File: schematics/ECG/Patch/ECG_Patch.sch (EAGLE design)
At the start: 7 parts

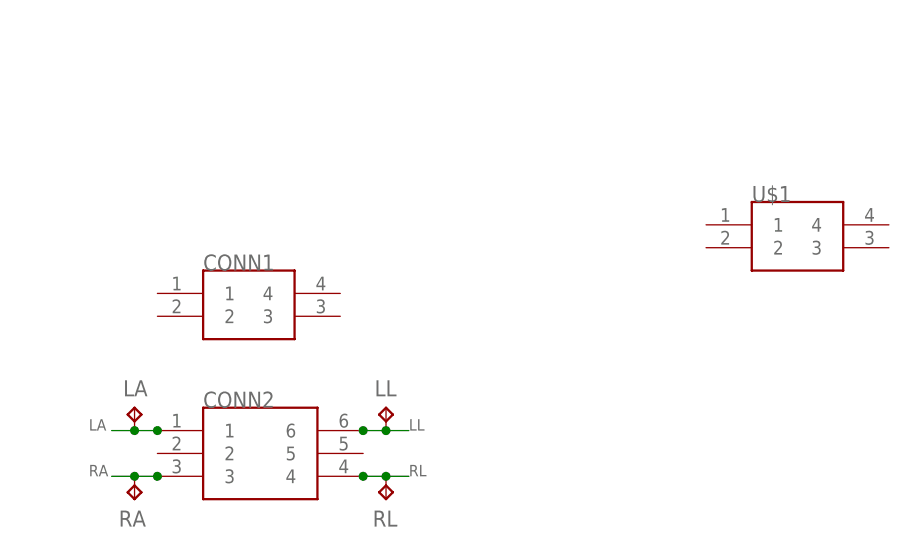
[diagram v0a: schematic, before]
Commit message: changed 4 pin to through hole and added v1.0 marking
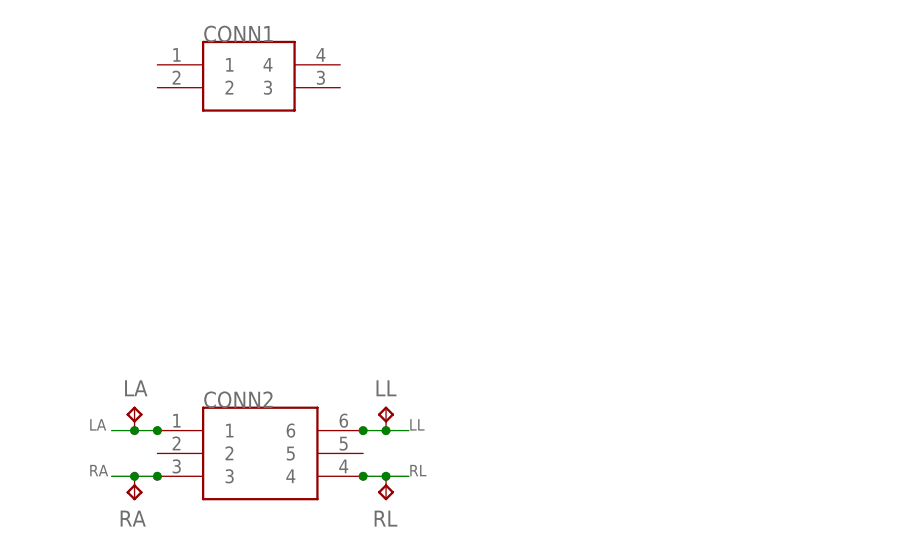
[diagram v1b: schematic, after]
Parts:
- removed U$1: M80-4SMT, harwin:M80-4SMT
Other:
- moved on the sheet: CONN1
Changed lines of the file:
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@@
 </classes>
 <parts>
-<part name="CONN1" library="harwin" deviceset="M80-4" device="V"/>
 <part name="CONN2" library="harwin" deviceset="M80-6" device="V"/>
 <part name="LL" library="testpad" deviceset="TP" device="TP20R"/>
@@
 <part name="RA" library="testpad" deviceset="TP" device="TP20R"/>
 <part name="RL" library="testpad" deviceset="TP" device="TP20R"/>
-<part name="U$1" library="harwin" deviceset="M80-4" device="SMT"/>
+<part name="CONN1" library="harwin" deviceset="M80-4" device="V"/>
 </parts>
 <sheets>
@@
 </plain>
 <instances>
-<instance part="CONN1" gate="CONN" x="22.86" y="55.88"/>
 <instance part="CONN2" gate="CONN" x="22.86" y="40.64"/>
 <instance part="LL" gate="G$1" x="38.1" y="45.72"/>
@@
 <instance part="RA" gate="G$1" x="10.16" y="35.56" rot="R180"/>
 <instance part="RL" gate="G$1" x="38.1" y="35.56" rot="R180"/>
-<instance part="U$1" gate="CONN" x="83.82" y="63.5"/>
+<instance part="CONN1" gate="CONN" x="22.86" y="81.28"/>
 </instances>
 <busses>

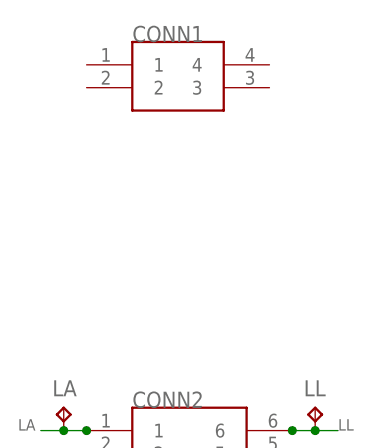
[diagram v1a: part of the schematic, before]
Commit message: switched ECG boards to spring loaded pin headers
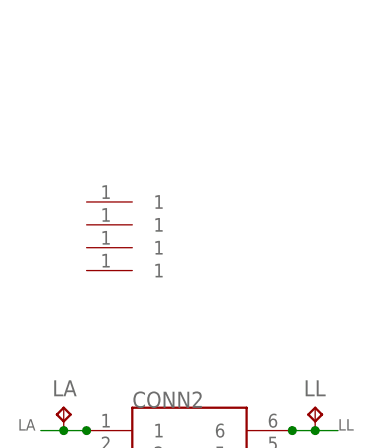
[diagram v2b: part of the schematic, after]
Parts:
- removed CONN1: M80-4V, harwin:M80-4V
- added U$1, U$2, U$3, U$4: PISTON_RA_TH, pins:PISTON_RA_TH
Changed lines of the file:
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@@
 <?xml version="1.0" encoding="utf-8"?>
 <!DOCTYPE eagle SYSTEM "eagle.dtd">
-<eagle version="6.4">
+<eagle version="6.5.0">
 <drawing>
 <settings>
@@
 <part name="RA" library="testpad" deviceset="TP" device="TP20R"/>
 <part name="RL" library="testpad" deviceset="TP" device="TP20R"/>
-<part name="CONN1" library="harwin" deviceset="M80-4" device="V"/>
+<part name="U$1" library="pins" deviceset="PISTON_RA_TH" device=""/>
+<part name="U$2" library="pins" deviceset="PISTON_RA_TH" device=""/>
+<part name="U$3" library="pins" deviceset="PISTON_RA_TH" device=""/>
+<part name="U$4" library="pins" deviceset="PISTON_RA_TH" device=""/>
 </parts>
 <sheets>
@@
 <instance part="RA" gate="G$1" x="10.16" y="35.56" rot="R180"/>
 <instance part="RL" gate="G$1" x="38.1" y="35.56" rot="R180"/>
-<instance part="CONN1" gate="CONN" x="22.86" y="81.28"/>
+<instance part="U$1" gate="PIN" x="17.78" y="66.04"/>
+<instance part="U$2" gate="PIN" x="17.78" y="68.58"/>
+<instance part="U$3" gate="PIN" x="17.78" y="63.5"/>
+<instance part="U$4" gate="PIN" x="17.78" y="60.96"/>
 </instances>
 <busses>

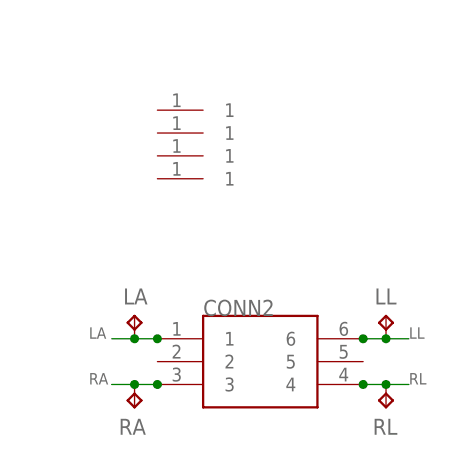
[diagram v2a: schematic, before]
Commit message: redesigned patch board and charging board
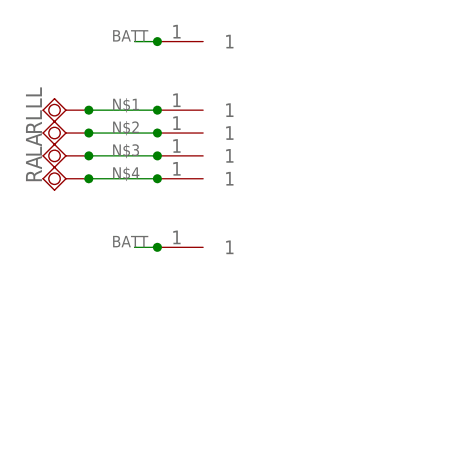
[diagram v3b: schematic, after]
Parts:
- removed CONN2: M80-6V, harwin:M80-6V
- added U$5, U$6: PISTON_RA_TH, pins:PISTON_RA_TH
- LA, LL, RA, RL: value TPTP20R -> TPSQPAD1-20; device testpad:TPTP20R -> testpad:TPSQPAD1-20
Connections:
- removed net LA: CONN2.1, LA.TP
- removed net LL: CONN2.6, LL.TP
- removed net RA: CONN2.3, RA.TP
- removed net RL: CONN2.4, RL.TP
- new net BATT: U$5.1, U$6.1
- new net N$1: LL.TP, U$2.1
- new net N$2: RL.TP, U$1.1
- new net N$3: LA.TP, U$3.1
- new net N$4: RA.TP, U$4.1
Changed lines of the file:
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@@
 </classes>
 <parts>
-<part name="CONN2" library="harwin" deviceset="M80-6" device="V"/>
-<part name="LL" library="testpad" deviceset="TP" device="TP20R"/>
-<part name="LA" library="testpad" deviceset="TP" device="TP20R"/>
-<part name="RA" library="testpad" deviceset="TP" device="TP20R"/>
-<part name="RL" library="testpad" deviceset="TP" device="TP20R"/>
 <part name="U$1" library="pins" deviceset="PISTON_RA_TH" device=""/>
 <part name="U$2" library="pins" deviceset="PISTON_RA_TH" device=""/>
 <part name="U$3" library="pins" deviceset="PISTON_RA_TH" device=""/>
 <part name="U$4" library="pins" deviceset="PISTON_RA_TH" device=""/>
+<part name="LL" library="testpad" deviceset="TPSQ" device="PAD1-20"/>
+<part name="RL" library="testpad" deviceset="TPSQ" device="PAD1-20"/>
+<part name="LA" library="testpad" deviceset="TPSQ" device="PAD1-20"/>
+<part name="RA" library="testpad" deviceset="TPSQ" device="PAD1-20"/>
+<part name="U$5" library="pins" deviceset="PISTON_RA_TH" device=""/>
+<part name="U$6" library="pins" deviceset="PISTON_RA_TH" device=""/>
 </parts>
 <sheets>
@@
 </plain>
 <instances>
-<instance part="CONN2" gate="CONN" x="22.86" y="40.64"/>
-<instance part="LL" gate="G$1" x="38.1" y="45.72"/>
-<instance part="LA" gate="G$1" x="10.16" y="45.72"/>
-<instance part="RA" gate="G$1" x="10.16" y="35.56" rot="R180"/>
-<instance part="RL" gate="G$1" x="38.1" y="35.56" rot="R180"/>
 <instance part="U$1" gate="PIN" x="17.78" y="66.04"/>
 <instance part="U$2" gate="PIN" x="17.78" y="68.58"/>
 <instance part="U$3" gate="PIN" x="17.78" y="63.5"/>
 <instance part="U$4" gate="PIN" x="17.78" y="60.96"/>
+<instance part="LL" gate="G$1" x="2.54" y="68.58" rot="R270"/>
+<instance part="RL" gate="G$1" x="2.54" y="66.04" rot="R270"/>
+<instance part="LA" gate="G$1" x="2.54" y="63.5" rot="R270"/>
+<instance part="RA" gate="G$1" x="2.54" y="60.96" rot="R270"/>
+<instance part="U$5" gate="PIN" x="17.78" y="76.2"/>
+<instance part="U$6" gate="PIN" x="17.78" y="53.34"/>
 </instances>
 <busses>
 </busses>
 <nets>
-<net name="LA" class="0">
+<net name="N$1" class="0">
 <segment>
-<pinref part="CONN2" gate="CONN" pin="1"/>
-<junction x="12.7" y="43.18"/>
-<label x="5.08" y="43.18" size="1.27" layer="95"/>
-<pinref part="LA" gate="G$1" pin="TP"/>
-<wire x1="12.7" y1="43.18" x2="10.16" y2="43.18" width="0.1524" layer="91"/>
-<wire x1="10.16" y1="43.18" x2="7.62" y2="43.18" width="0.1524" layer="91"/>
-<junction x="10.16" y="43.18"/>
+<pinref part="U$2" gate="PIN" pin="1"/>
+<pinref part="LL" gate="G$1" pin="TP"/>
+<wire x1="12.7" y1="68.58" x2="5.08" y2="68.58" width="0.1524" layer="91"/>
+<junction x="5.08" y="68.58"/>
+<junction x="12.7" y="68.58"/>
+<label x="7.62" y="68.58" size="1.27" layer="95"/>
 </segment>
 </net>
-<net name="RL" class="0">
+<net name="N$2" class="0">
 <segment>
-<label x="40.64" y="38.1" size="1.27" layer="95"/>
+<pinref part="U$1" gate="PIN" pin="1"/>
 <pinref part="RL" gate="G$1" pin="TP"/>
-<wire x1="38.1" y1="38.1" x2="40.64" y2="38.1" width="0.1524" layer="91"/>
-<pinref part="CONN2" gate="CONN" pin="4"/>
-<wire x1="38.1" y1="38.1" x2="35.56" y2="38.1" width="0.1524" layer="91"/>
-<junction x="38.1" y="38.1"/>
-<junction x="35.56" y="38.1"/>
+<wire x1="12.7" y1="66.04" x2="5.08" y2="66.04" width="0.1524" layer="91"/>
+<junction x="5.08" y="66.04"/>
+<junction x="12.7" y="66.04"/>
+<label x="7.62" y="66.04" size="1.27" layer="95"/>
 </segment>
 </net>
-<net name="LL" class="0">
+<net name="N$3" class="0">
 <segment>
-<pinref part="CONN2" gate="CONN" pin="6"/>
-<wire x1="35.56" y1="43.18" x2="38.1" y2="43.18" width="0.1524" layer="91"/>
-<junction x="35.56" y="43.18"/>
-<label x="40.64" y="43.18" size="1.27" layer="95"/>
-<pinref part="LL" gate="G$1" pin="TP"/>
-<wire x1="38.1" y1="43.18" x2="40.64" y2="43.18" width="0.1524" layer="91"/>
-<junction x="38.1" y="43.18"/>
+<pinref part="U$3" gate="PIN" pin="1"/>
+<pinref part="LA" gate="G$1" pin="TP"/>
+<wire x1="12.7" y1="63.5" x2="5.08" y2="63.5" width="0.1524" layer="91"/>
+<junction x="5.08" y="63.5"/>
+<junction x="12.7" y="63.5"/>
+<label x="7.62" y="63.5" size="1.27" layer="95"/>
 </segment>
 </net>
-<net name="RA" class="0">
+<net name="N$4" class="0">
 <segment>
-<wire x1="10.16" y1="38.1" x2="7.62" y2="38.1" width="0.1524" layer="91"/>
+<pinref part="U$4" gate="PIN" pin="1"/>
 <pinref part="RA" gate="G$1" pin="TP"/>
-<label x="5.08" y="38.1" size="1.27" layer="95"/>
-<pinref part="CONN2" gate="CONN" pin="3"/>
-<wire x1="10.16" y1="38.1" x2="12.7" y2="38.1" width="0.1524" layer="91"/>
-<junction x="10.16" y="38.1"/>
-<junction x="12.7" y="38.1"/>
+<wire x1="12.7" y1="60.96" x2="5.08" y2="60.96" width="0.1524" layer="91"/>
+<junction x="5.08" y="60.96"/>
+<junction x="12.7" y="60.96"/>
+<label x="7.62" y="60.96" size="1.27" layer="95"/>
 </segment>
 </net>
+<net name="BATT" class="0">
+<segment>
+<pinref part="U$5" gate="PIN" pin="1"/>
+<wire x1="12.7" y1="76.2" x2="10.16" y2="76.2" width="0.1524" layer="91"/>
+<junction x="12.7" y="76.2"/>
+<label x="7.62" y="76.2" size="1.27" layer="95"/>
+</segment>
+<segment>
+<pinref part="U$6" gate="PIN" pin="1"/>
+<wire x1="12.7" y1="53.34" x2="10.16" y2="53.34" width="0.1524" layer="91"/>
+<junction x="12.7" y="53.34"/>
+<label x="7.62" y="53.34" size="1.27" layer="95"/>
+</segment>
+</net>

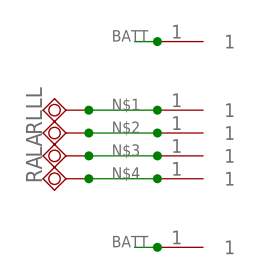
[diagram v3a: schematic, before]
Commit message: scaled down patch pcb. Same dimensions as charger board
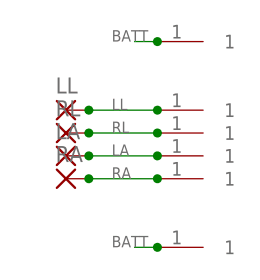
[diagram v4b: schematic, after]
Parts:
- LA, LL, RA, RL: value TPSQPAD1-20 -> (none); device testpad:TPSQPAD1-20 -> wirepad:1,6/0,8
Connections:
- removed net N$1: LL.TP, U$2.1
- removed net N$2: RL.TP, U$1.1
- removed net N$3: LA.TP, U$3.1
- removed net N$4: RA.TP, U$4.1
- new net LA: LA.P, U$3.1
- new net LL: LL.P, U$2.1
- new net RA: RA.P, U$4.1
- new net RL: RL.P, U$1.1
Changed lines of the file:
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@@
 <?xml version="1.0" encoding="utf-8"?>
 <!DOCTYPE eagle SYSTEM "eagle.dtd">
-<eagle version="6.5.0">
+<eagle version="6.4">
 <drawing>
 <settings>
@@
 <grid distance="0.1" unitdist="inch" unit="inch" style="lines" multiple="1" display="no" altdistance="0.01" altunitdist="inch" altunit="inch"/>
 <layers>
-<layer number="1" name="Top" color="4" fill="1" visible="no" active="no"/>
-<layer number="2" name="Route2" color="1" fill="3" visible="no" active="no"/>
-<layer number="3" name="Route3" color="4" fill="3" visible="no" active="no"/>
-<layer number="14" name="Route14" color="1" fill="6" visible="no" active="no"/>
-<layer number="15" name="Route15" color="4" fill="6" visible="no" active="no"/>
-<layer number="16" name="Bottom" color="1" fill="1" visible="no" active="no"/>
-<layer number="17" name="Pads" color="2" fill="1" visible="no" active="no"/>
-<layer number="18" name="Vias" color="2" fill="1" visible="no" active="no"/>
-<layer number="19" name="Unrouted" color="6" fill="1" visible="no" active="no"/>
-<layer number="20" name="Dimension" color="15" fill="1" visible="no" active="no"/>
-<layer number="21" name="tPlace" color="7" fill="1" visible="no" active="no"/>
-<layer number="22" name="bPlace" color="7" fill="1" visible="no" active="no"/>
-<layer number="23" name="tOrigins" color="15" fill="1" visible="no" active="no"/>
-<layer number="24" name="bOrigins" color="15" fill="1" visible="no" active="no"/>
-<layer number="25" name="tNames" color="7" fill="1" visible="no" active="no"/>
-<layer number="26" name="bNames" color="7" fill="1" visible="no" active="no"/>
-<layer number="27" name="tValues" color="7" fill="1" visible="no" active="no"/>
-<layer number="28" name="bValues" color="7" fill="1" visible="no" active="no"/>
+<layer number="1" name="Top" color="4" fill="1" visible="yes" active="no"/>
+<layer number="2" name="Route2" color="1" fill="3" visible="yes" active="no"/>
+<layer number="3" name="Route3" color="4" fill="3" visible="yes" active="no"/>
+<layer number="14" name="Route14" color="1" fill="6" visible="yes" active="no"/>
+<layer number="15" name="Route15" color="4" fill="6" visible="yes" active="no"/>
+<layer number="16" name="Bottom" color="1" fill="1" visible="yes" active="no"/>
+<layer number="17" name="Pads" color="2" fill="1" visible="yes" active="no"/>
+<layer number="18" name="Vias" color="2" fill="1" visible="yes" active="no"/>
+<layer number="19" name="Unrouted" color="6" fill="1" visible="yes" active="no"/>
+<layer number="20" name="Dimension" color="15" fill="1" visible="yes" active="no"/>
+<layer number="21" name="tPlace" color="7" fill="1" visible="yes" active="no"/>
+<layer number="22" name="bPlace" color="7" fill="1" visible="yes" active="no"/>
+<layer number="23" name="tOrigins" color="15" fill="1" visible="yes" active="no"/>
+<layer number="24" name="bOrigins" color="15" fill="1" visible="yes" active="no"/>
+<layer number="25" name="tNames" color="7" fill="1" visible="yes" active="no"/>
+<layer number="26" name="bNames" color="7" fill="1" visible="yes" active="no"/>
+<layer number="27" name="tValues" color="7" fill="1" visible="yes" active="no"/>
+<layer number="28" name="bValues" color="7" fill="1" visible="yes" active="no"/>
 <layer number="29" name="tStop" color="7" fill="3" visible="no" active="no"/>
 <layer number="30" name="bStop" color="7" fill="6" visible="no" active="no"/>
@@
 <layer number="35" name="tGlue" color="7" fill="4" visible="no" active="no"/>
 <layer number="36" name="bGlue" color="7" fill="5" visible="no" active="no"/>
-<layer number="37" name="tTest" color="7" fill="1" visible="no" active="no"/>
-<layer number="38" name="bTest" color="7" fill="1" visible="no" active="no"/>
+<layer number="37" name="tTest" color="7" fill="1" visible="yes" active="no"/>
+<layer number="38" name="bTest" color="7" fill="1" visible="yes" active="no"/>
 <layer number="39" name="tKeepout" color="4" fill="11" visible="no" active="no"/>
 <layer number="40" name="bKeepout" color="1" fill="11" visible="no" active="no"/>
@@
 <layer number="44" name="Drills" color="7" fill="1" visible="no" active="no"/>
 <layer number="45" name="Holes" color="7" fill="1" visible="no" active="no"/>
-<layer number="46" name="Milling" color="3" fill="1" visible="no" active="no"/>
-<layer number="47" name="Measures" color="7" fill="1" visible="no" active="no"/>
-<layer number="48" name="Document" color="7" fill="1" visible="no" active="no"/>
-<layer number="49" name="Reference" color="7" fill="1" visible="no" active="no"/>
-<layer number="50" name="dxf" color="7" fill="1" visible="no" active="no"/>
-<layer number="51" name="tDocu" color="7" fill="1" visible="no" active="no"/>
-<layer number="52" name="bDocu" color="7" fill="1" visible="no" active="no"/>
-<layer number="53" name="tGND_GNDA" color="7" fill="1" visible="no" active="no"/>
-<layer number="54" name="bGND_GNDA" color="7" fill="1" visible="no" active="no"/>
-<layer number="56" name="wert" color="7" fill="1" visible="no" active="no"/>
+<layer number="46" name="Milling" color="3" fill="1" visible="yes" active="no"/>
+<layer number="47" name="Measures" color="7" fill="1" visible="yes" active="no"/>
+<layer number="48" name="Document" color="7" fill="1" visible="yes" active="no"/>
+<layer number="49" name="Reference" color="7" fill="1" visible="yes" active="no"/>
+<layer number="50" name="dxf" color="7" fill="1" visible="yes" active="no"/>
+<layer number="51" name="tDocu" color="7" fill="1" visible="yes" active="no"/>
+<layer number="52" name="bDocu" color="7" fill="1" visible="yes" active="no"/>
+<layer number="53" name="tGND_GNDA" color="7" fill="1" visible="yes" active="no"/>
+<layer number="54" name="bGND_GNDA" color="7" fill="1" visible="yes" active="no"/>
+<layer number="56" name="wert" color="7" fill="1" visible="yes" active="no"/>
 <layer number="91" name="Nets" color="2" fill="1" visible="yes" active="yes"/>
 <layer number="92" name="Busses" color="1" fill="1" visible="yes" active="yes"/>
@@
 <part name="U$3" library="pins" deviceset="PISTON_RA_TH" device=""/>
 <part name="U$4" library="pins" deviceset="PISTON_RA_TH" device=""/>
-<part name="LL" library="testpad" deviceset="TPSQ" device="PAD1-20"/>
-<part name="RL" library="testpad" deviceset="TPSQ" device="PAD1-20"/>
-<part name="LA" library="testpad" deviceset="TPSQ" device="PAD1-20"/>
-<part name="RA" library="testpad" deviceset="TPSQ" device="PAD1-20"/>
 <part name="U$5" library="pins" deviceset="PISTON_RA_TH" device=""/>
 <part name="U$6" library="pins" deviceset="PISTON_RA_TH" device=""/>
+<part name="LL" library="wirepad" deviceset="1,6/0,8" device=""/>
+<part name="RL" library="wirepad" deviceset="1,6/0,8" device=""/>
+<part name="LA" library="wirepad" deviceset="1,6/0,8" device=""/>
+<part name="RA" library="wirepad" deviceset="1,6/0,8" device=""/>
 </parts>
 <sheets>
@@
 <instance part="U$3" gate="PIN" x="17.78" y="63.5"/>
 <instance part="U$4" gate="PIN" x="17.78" y="60.96"/>
-<instance part="LL" gate="G$1" x="2.54" y="68.58" rot="R270"/>
-<instance part="RL" gate="G$1" x="2.54" y="66.04" rot="R270"/>
-<instance part="LA" gate="G$1" x="2.54" y="63.5" rot="R270"/>
-<instance part="RA" gate="G$1" x="2.54" y="60.96" rot="R270"/>
 <instance part="U$5" gate="PIN" x="17.78" y="76.2"/>
 <instance part="U$6" gate="PIN" x="17.78" y="53.34"/>
+<instance part="LL" gate="P" x="2.54" y="68.58"/>
+<instance part="RL" gate="P" x="2.54" y="66.04"/>
+<instance part="LA" gate="P" x="2.54" y="63.5"/>
+<instance part="RA" gate="P" x="2.54" y="60.96"/>
 </instances>
 <busses>
 </busses>
 <nets>
-<net name="N$1" class="0">
+<net name="LL" class="0">
 <segment>
 <pinref part="U$2" gate="PIN" pin="1"/>
-<pinref part="LL" gate="G$1" pin="TP"/>
 <wire x1="12.7" y1="68.58" x2="5.08" y2="68.58" width="0.1524" layer="91"/>
-<junction x="5.08" y="68.58"/>
 <junction x="12.7" y="68.58"/>
 <label x="7.62" y="68.58" size="1.27" layer="95"/>
+<pinref part="LL" gate="P" pin="P"/>
+<junction x="5.08" y="68.58"/>
 </segment>
 </net>
-<net name="N$2" class="0">
+<net name="RL" class="0">
 <segment>
 <pinref part="U$1" gate="PIN" pin="1"/>
-<pinref part="RL" gate="G$1" pin="TP"/>
 <wire x1="12.7" y1="66.04" x2="5.08" y2="66.04" width="0.1524" layer="91"/>
-<junction x="5.08" y="66.04"/>
 <junction x="12.7" y="66.04"/>
 <label x="7.62" y="66.04" size="1.27" layer="95"/>
+<pinref part="RL" gate="P" pin="P"/>
+<junction x="5.08" y="66.04"/>
 </segment>
 </net>
-<net name="N$3" class="0">
+<net name="LA" class="0">
 <segment>
 <pinref part="U$3" gate="PIN" pin="1"/>
-<pinref part="LA" gate="G$1" pin="TP"/>
 <wire x1="12.7" y1="63.5" x2="5.08" y2="63.5" width="0.1524" layer="91"/>
-<junction x="5.08" y="63.5"/>
 <junction x="12.7" y="63.5"/>
 <label x="7.62" y="63.5" size="1.27" layer="95"/>
+<pinref part="LA" gate="P" pin="P"/>
+<junction x="5.08" y="63.5"/>
 </segment>
 </net>
-<net name="N$4" class="0">
+<net name="RA" class="0">
 <segment>
 <pinref part="U$4" gate="PIN" pin="1"/>
-<pinref part="RA" gate="G$1" pin="TP"/>
 <wire x1="12.7" y1="60.96" x2="5.08" y2="60.96" width="0.1524" layer="91"/>
-<junction x="5.08" y="60.96"/>
 <junction x="12.7" y="60.96"/>
 <label x="7.62" y="60.96" size="1.27" layer="95"/>
+<pinref part="RA" gate="P" pin="P"/>
+<junction x="5.08" y="60.96"/>
 </segment>
 </net>
